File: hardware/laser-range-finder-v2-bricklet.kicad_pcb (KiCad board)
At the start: 2 copper layers, 48.2 x 35.6 mm, 27 parts, among them P1 CON-SENSOR2, P2 DEBUG, P3 BOOT, P4 JST_GHR_6, U1 XMC1XXX24, U2 DRILL, U3 DRILL, U4 DRILL, U5 DRILL

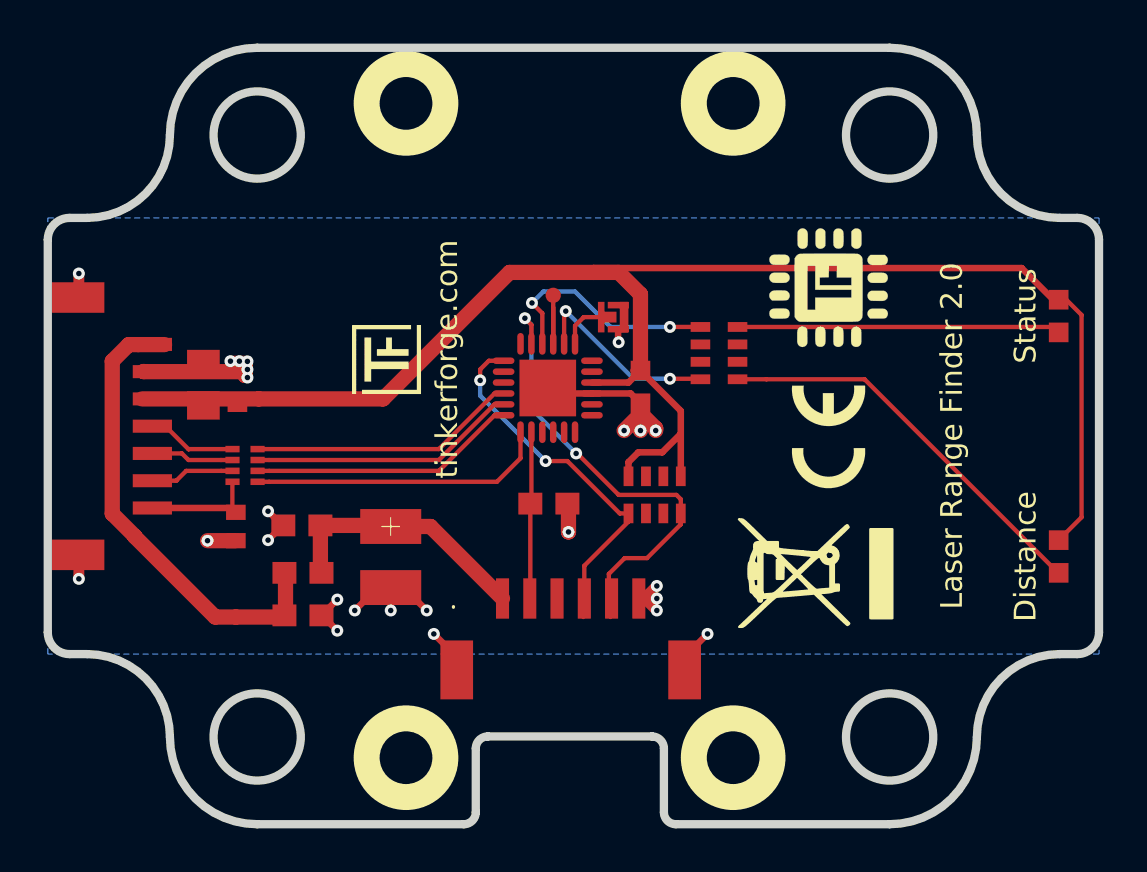
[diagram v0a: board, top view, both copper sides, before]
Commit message: add fiducials, fix drc bugs, optimize routing
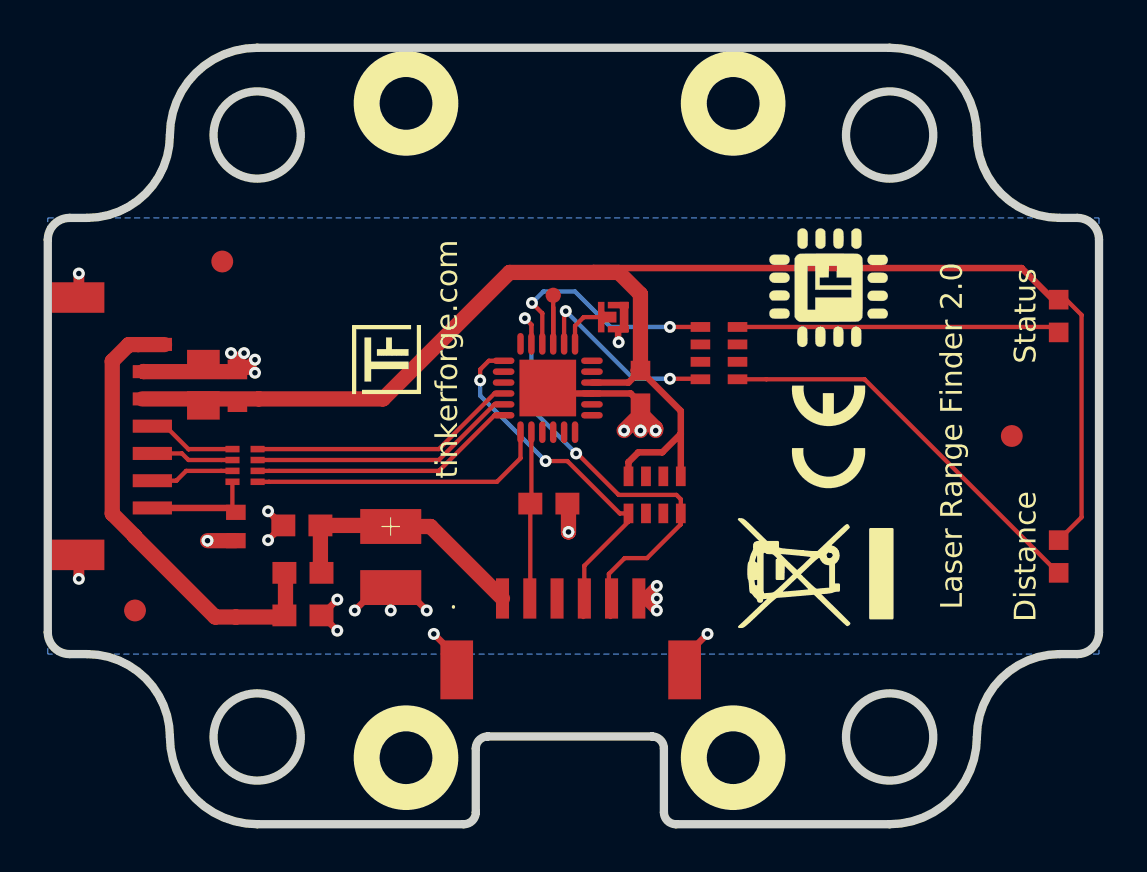
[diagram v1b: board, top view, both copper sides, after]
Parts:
- added Fiducial_Mark: VAL**, kicad-libraries:Fiducial_Mark, F.Cu at (118.5, 95.7)
- added Fiducial_Mark: VAL**, kicad-libraries:Fiducial_Mark, F.Cu at (154.7, 103.7)
- added Fiducial_Mark: VAL**, kicad-libraries:Fiducial_Mark, F.Cu at (114.5, 111.7)
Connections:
- P4 pad 3: Net-(P4-Pad3) -> (no net)
- RP2 pad 2: Net-(RP2-Pad2) -> (no net)
- RP2 pad 3: Net-(RP2-Pad3) -> (no net)
- RP2 pad 6: Net-(RP2-Pad6) -> (no net)
- RP2 pad 7: Net-(RP2-Pad7) -> (no net)
- RP3 pad 2: Net-(RP3-Pad2) -> (no net)
- RP3 pad 3: Net-(RP3-Pad3) -> (no net)
- RP3 pad 5: Net-(RP3-Pad5) -> 3V3
- RP3 pad 6: Net-(RP3-Pad6) -> (no net)
- RP3 pad 7: Net-(RP3-Pad7) -> (no net)
- RP3 pad 8: Net-(RP3-Pad5) -> 3V3
- U1 pad 11: Net-(U1-Pad11) -> (no net)
- U1 pad 12: Net-(U1-Pad12) -> (no net)
- U1 pad 18: Net-(U1-Pad18) -> (no net)
- U1 pad 20: Net-(U1-Pad20) -> (no net)
- U1 pad 21: Net-(U1-Pad21) -> (no net)
- U1 pad 3: Net-(U1-Pad3) -> (no net)
- U1 pad 4: Net-(U1-Pad4) -> (no net)
- U1 pad 5: Net-(U1-Pad5) -> (no net)
- U1 pad 6: Net-(U1-Pad6) -> (no net)
- U1 pad 7: Net-(U1-Pad7) -> (no net)
- U1 pad 8: Net-(U1-Pad8) -> (no net)
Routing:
- net GND: track 46.4 -> 47.8 mm, vias 25 -> 24

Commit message: add schematic
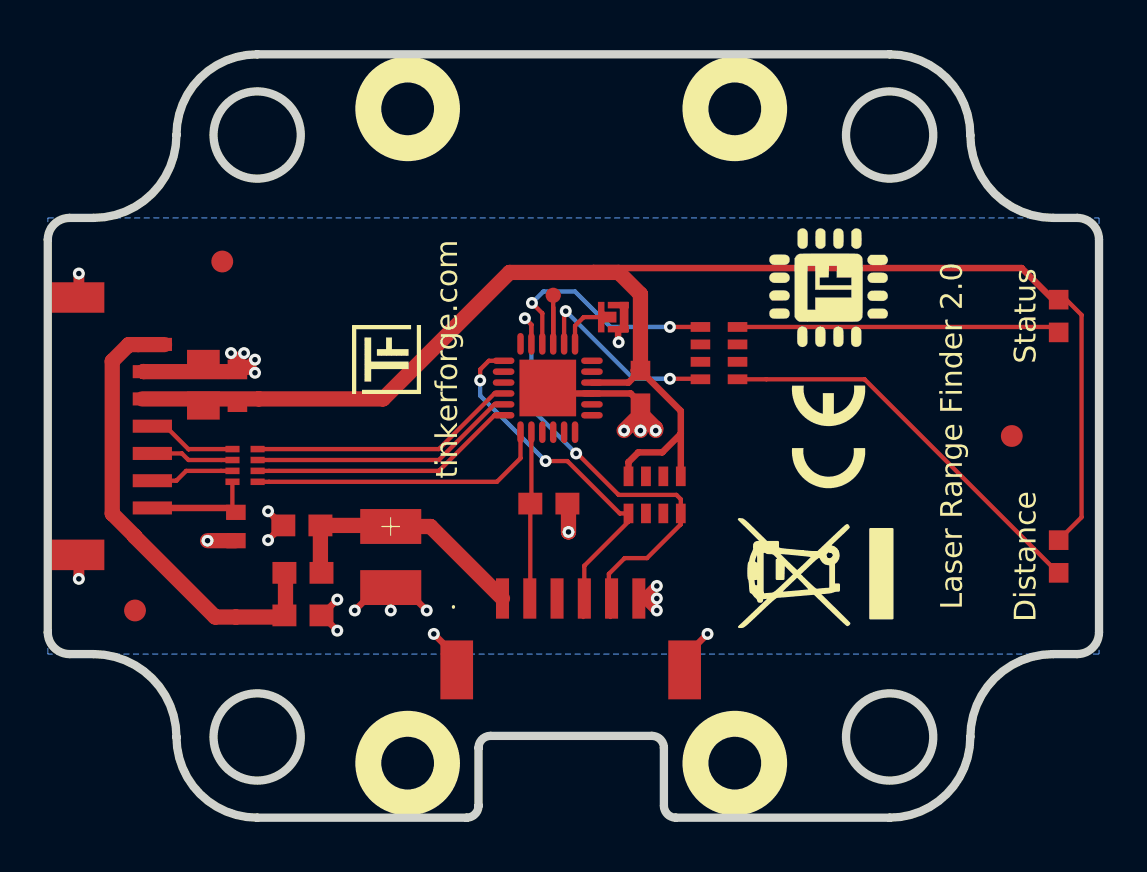
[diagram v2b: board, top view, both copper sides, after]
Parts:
- moved U2 0.26 mm to (127.0, 118.7)
- moved U4 0.26 mm to (127.0, 88.7)
- moved U3 0.26 mm to (141.9, 118.7)
- moved U5 0.26 mm to (141.9, 88.7)
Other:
- board size 48.2 x 35.6 mm -> 48.2 x 35 mm
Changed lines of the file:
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@@
     (38 B.Mask user)
     (39 F.Mask user)
-    (40 Dwgs.User user)
+    (40 Dwgs.User user hide)
     (41 Cmts.User user)
     (42 Eco1.User user)
@@
   )
   (setup
-    (last_trace_width 0.5)
+    (last_trace_width 0.2)
     (user_trace_width 0.29972)
     (user_trace_width 0.3)
@@
   )
   (module DRILL_NP (layer Vorderseite)
-    (at 126.875 118.4)
+    (at 126.95 118.65)
     (fp_text reference U2 (at 0 0) (layer F.SilkS) hide
       (effects (font (size 0.29972 0.29972) (thickness 0.0762)))
@@
   )
   (module DRILL_NP (layer Vorderseite)
-    (at 141.875 118.4)
+    (at 141.95 118.65)
     (fp_text reference U3 (at 0 0) (layer F.SilkS) hide
       (effects (font (size 0.29972 0.29972) (thickness 0.0762)))
@@
   )
   (module DRILL_NP (layer Vorderseite)
-    (at 126.875 88.4)
+    (at 126.95 88.65)
     (fp_text reference U4 (at 0 0) (layer F.SilkS) hide
       (effects (font (size 0.29972 0.29972) (thickness 0.0762)))
@@
   )
   (module DRILL_NP (layer Vorderseite)
-    (at 141.875 88.4)
+    (at 141.95 88.65)
     (fp_text reference U5 (at 0 0) (layer F.SilkS) hide
       (effects (font (size 0.29972 0.29972) (thickness 0.0762)))
@@
       (clearance 0.65024))
   )
+  (gr_line (start 130.75 117.4) (end 138.15 117.4) (angle 90) (layer Edge.Cuts) (width 0.381))
+  (gr_arc (start 130.75 117.95) (end 130.2 117.95) (angle 90) (layer Edge.Cuts) (width 0.381))
+  (gr_arc (start 138.15 117.95) (end 138.15 117.4) (angle 90) (layer Edge.Cuts) (width 0.381))
+  (gr_line (start 130.2 117.95) (end 130.2 120.6) (angle 90) (layer Edge.Cuts) (width 0.381))
+  (gr_line (start 138.7 120.6) (end 138.7 117.95) (angle 90) (layer Edge.Cuts) (width 0.381))
+  (gr_arc (start 129.65 120.6) (end 130.2 120.6) (angle 90) (layer Edge.Cuts) (width 0.381))
+  (gr_arc (start 139.25 120.6) (end 139.25 121.15) (angle 90) (layer Edge.Cuts) (width 0.381))
+  (gr_line (start 120.05 121.15) (end 129.65 121.15) (angle 90) (layer Edge.Cuts) (width 0.381))
+  (gr_line (start 112.55 93.65) (end 111.45 93.65) (angle 90) (layer Edge.Cuts) (width 0.381))
+  (gr_line (start 157.65 93.65) (end 156.55 93.65) (angle 90) (layer Edge.Cuts) (width 0.381))
+  (gr_arc (start 156.55 89.85) (end 156.55 93.65) (angle 90) (layer Edge.Cuts) (width 0.381))
+  (gr_arc (start 112.55 89.85) (end 116.35 89.85) (angle 90) (layer Edge.Cuts) (width 0.381))
+  (gr_arc (start 120.05 89.85) (end 116.35 89.85) (angle 90) (layer Edge.Cuts) (width 0.381))
+  (gr_arc (start 149.05 89.85) (end 149.05 86.15) (angle 90) (layer Edge.Cuts) (width 0.381))
+  (gr_line (start 157.65 113.65) (end 156.55 113.65) (angle 90) (layer Edge.Cuts) (width 0.381))
+  (gr_line (start 112.55 113.65) (end 111.45 113.65) (angle 90) (layer Edge.Cuts) (width 0.381))
+  (gr_arc (start 112.55 117.45) (end 112.55 113.65) (angle 90) (layer Edge.Cuts) (width 0.381))
+  (gr_arc (start 156.55 117.45) (end 152.75 117.45) (angle 90) (layer Edge.Cuts) (width 0.381))
+  (gr_arc (start 149.05 117.45) (end 152.75 117.45) (angle 90) (layer Edge.Cuts) (width 0.381))
+  (gr_arc (start 120.05 117.45) (end 120.05 121.15) (angle 90) (layer Edge.Cuts) (width 0.381))
   (gr_text tinkerforge.com (at 128.75 100.125 90) (layer F.SilkS)
     (effects (font (size 1 1) (thickness 0.15)))
@@
     (effects (font (size 1 1) (thickness 0.15)))
   )
-  (gr_line (start 129.525 121.45) (end 120.05 121.45) (angle 90) (layer Edge.Cuts) (width 0.381))
-  (gr_line (start 130.075 117.975) (end 130.075 120.9) (angle 90) (layer Edge.Cuts) (width 0.381))
-  (gr_arc (start 129.525 120.9) (end 130.075 120.9) (angle 90) (layer Edge.Cuts) (width 0.381))
-  (gr_line (start 139.25 121.45) (end 149.05 121.45) (angle 90) (layer Edge.Cuts) (width 0.381))
-  (gr_line (start 138.7 117.975) (end 138.7 120.9) (angle 90) (layer Edge.Cuts) (width 0.381))
-  (gr_line (start 130.625 117.425) (end 138.15 117.425) (angle 90) (layer Edge.Cuts) (width 0.381))
-  (gr_arc (start 139.25 120.9) (end 139.25 121.45) (angle 90) (layer Edge.Cuts) (width 0.381))
-  (gr_arc (start 138.15 117.975) (end 138.15 117.425) (angle 90) (layer Edge.Cuts) (width 0.381))
-  (gr_arc (start 130.625 117.975) (end 130.075 117.975) (angle 90) (layer Edge.Cuts) (width 0.381))
-  (gr_arc (start 149.05 117.45) (end 153.05 117.45) (angle 90) (layer Edge.Cuts) (width 0.381))
-  (gr_arc (start 120.05 117.45) (end 120.05 121.45) (angle 90) (layer Edge.Cuts) (width 0.381))
-  (gr_arc (start 112.25 117.45) (end 112.25 113.65) (angle 90) (layer Edge.Cuts) (width 0.381))
+  (gr_line (start 139.25 121.15) (end 149.05 121.15) (angle 90) (layer Edge.Cuts) (width 0.381))
   (gr_line (start 157.2 113.65) (end 112.35 113.65) (angle 90) (layer Dwgs.User) (width 0.381))
   (gr_line (start 111.65 93.65) (end 156.7 93.65) (angle 90) (layer Dwgs.User) (width 0.381))
-  (gr_line (start 120.05 85.85) (end 149.05 85.85) (angle 90) (layer Edge.Cuts) (width 0.381))
-  (gr_line (start 112.25 113.65) (end 111.45 113.65) (angle 90) (layer Edge.Cuts) (width 0.381))
-  (gr_line (start 157.65 113.65) (end 156.85 113.65) (angle 90) (layer Edge.Cuts) (width 0.381))
+  (gr_line (start 120.05 86.15) (end 149.05 86.15) (angle 90) (layer Edge.Cuts) (width 0.381))
   (gr_line (start 158.65 94.65) (end 158.65 112.65) (angle 90) (layer Edge.Cuts) (width 0.381))
-  (gr_line (start 156.85 93.65) (end 157.65 93.65) (angle 90) (layer Edge.Cuts) (width 0.381))
-  (gr_line (start 111.45 93.65) (end 112.25 93.65) (angle 90) (layer Edge.Cuts) (width 0.381))
   (gr_line (start 110.45 112.65) (end 110.45 94.65) (angle 90) (layer Edge.Cuts) (width 0.381))
   (gr_arc (start 111.45 112.65) (end 111.45 113.65) (angle 90) (layer Edge.Cuts) (width 0.381))
@@
   (gr_arc (start 157.65 94.65) (end 157.65 93.65) (angle 90) (layer Edge.Cuts) (width 0.381))
   (gr_arc (start 111.45 94.65) (end 110.45 94.65) (angle 90) (layer Edge.Cuts) (width 0.381))
-  (gr_arc (start 156.85 117.45) (end 153.05 117.45) (angle 90) (layer Edge.Cuts) (width 0.381))
-  (gr_arc (start 112.25 89.85) (end 116.05 89.85) (angle 90) (layer Edge.Cuts) (width 0.381))
-  (gr_arc (start 156.85 89.85) (end 156.85 93.65) (angle 90) (layer Edge.Cuts) (width 0.381))
-  (gr_arc (start 149.05 89.85) (end 149.05 85.85) (angle 90) (layer Edge.Cuts) (width 0.381))
-  (gr_arc (start 120.05 89.85) (end 116.05 89.85) (angle 90) (layer Edge.Cuts) (width 0.381))
   (gr_circle (center 149.05 117.45) (end 151.05 117.45) (layer Edge.Cuts) (width 0.381))
   (gr_circle (center 120.05 117.45) (end 118.05 117.45) (layer Edge.Cuts) (width 0.381))
